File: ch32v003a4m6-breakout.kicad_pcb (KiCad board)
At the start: 2 copper layers, 24.1 x 21.6 mm, 4 parts, among them J1 Conn_01x08, J2 Conn_01x08, U1 CH32V003A4M6

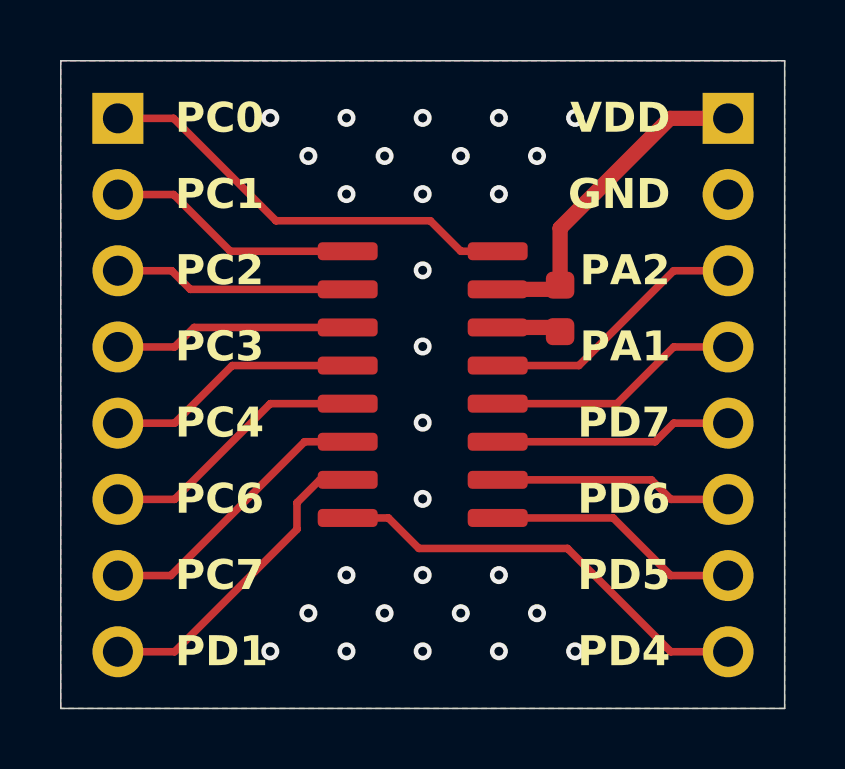
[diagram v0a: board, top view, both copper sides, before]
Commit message: fix: use default KiCad libraries
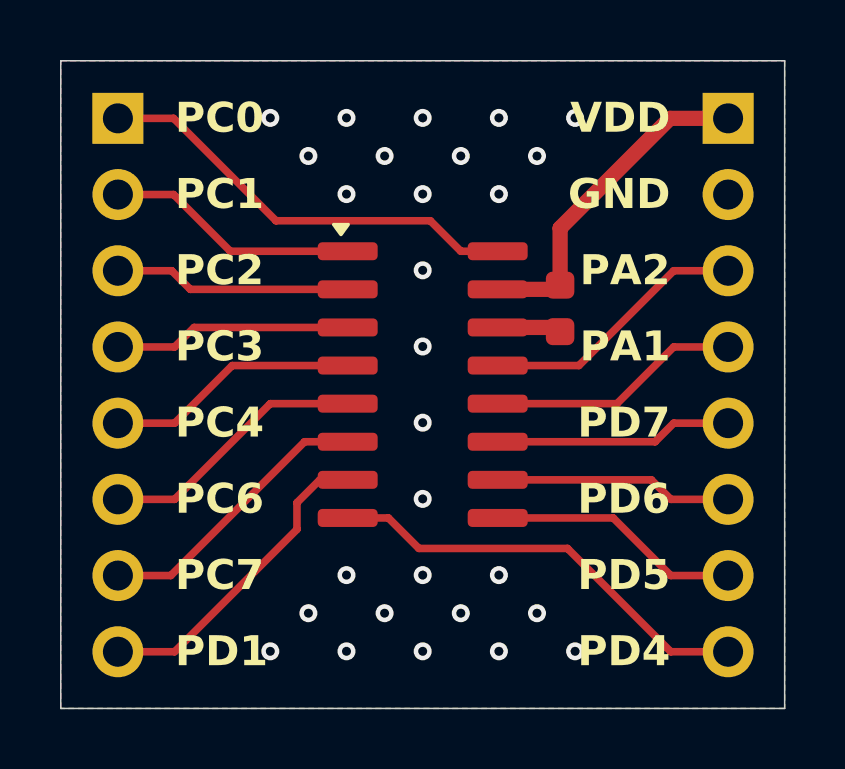
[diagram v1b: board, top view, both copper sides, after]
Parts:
- C1: value CL10A105KA8NNNC -> 1uF
- J1, J2: footprint Connector_PinHeader:PinHeader_1x08_P2.54mm_Vertical -> Connector_PinHeader_2.54mm:PinHeader_1x08_P2.54mm_Vertical
- turned C1 to 90 degrees
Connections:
- C1 pad 1: VDD -> GND
- C1 pad 2: GND -> VDD
